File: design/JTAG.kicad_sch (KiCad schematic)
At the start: 46 parts

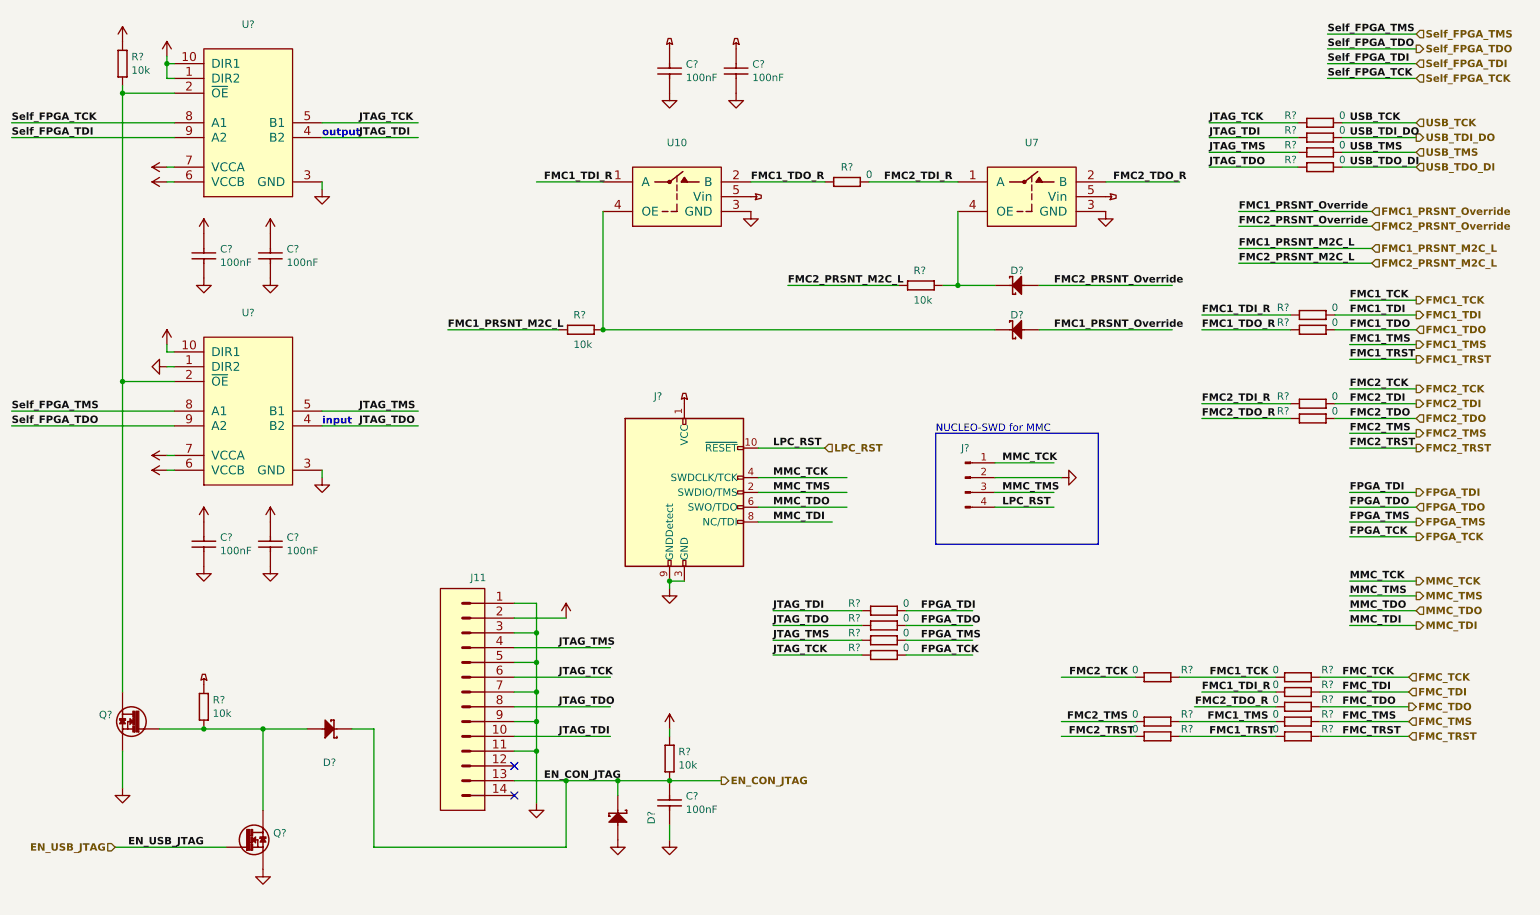
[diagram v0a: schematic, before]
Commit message: new power converter added
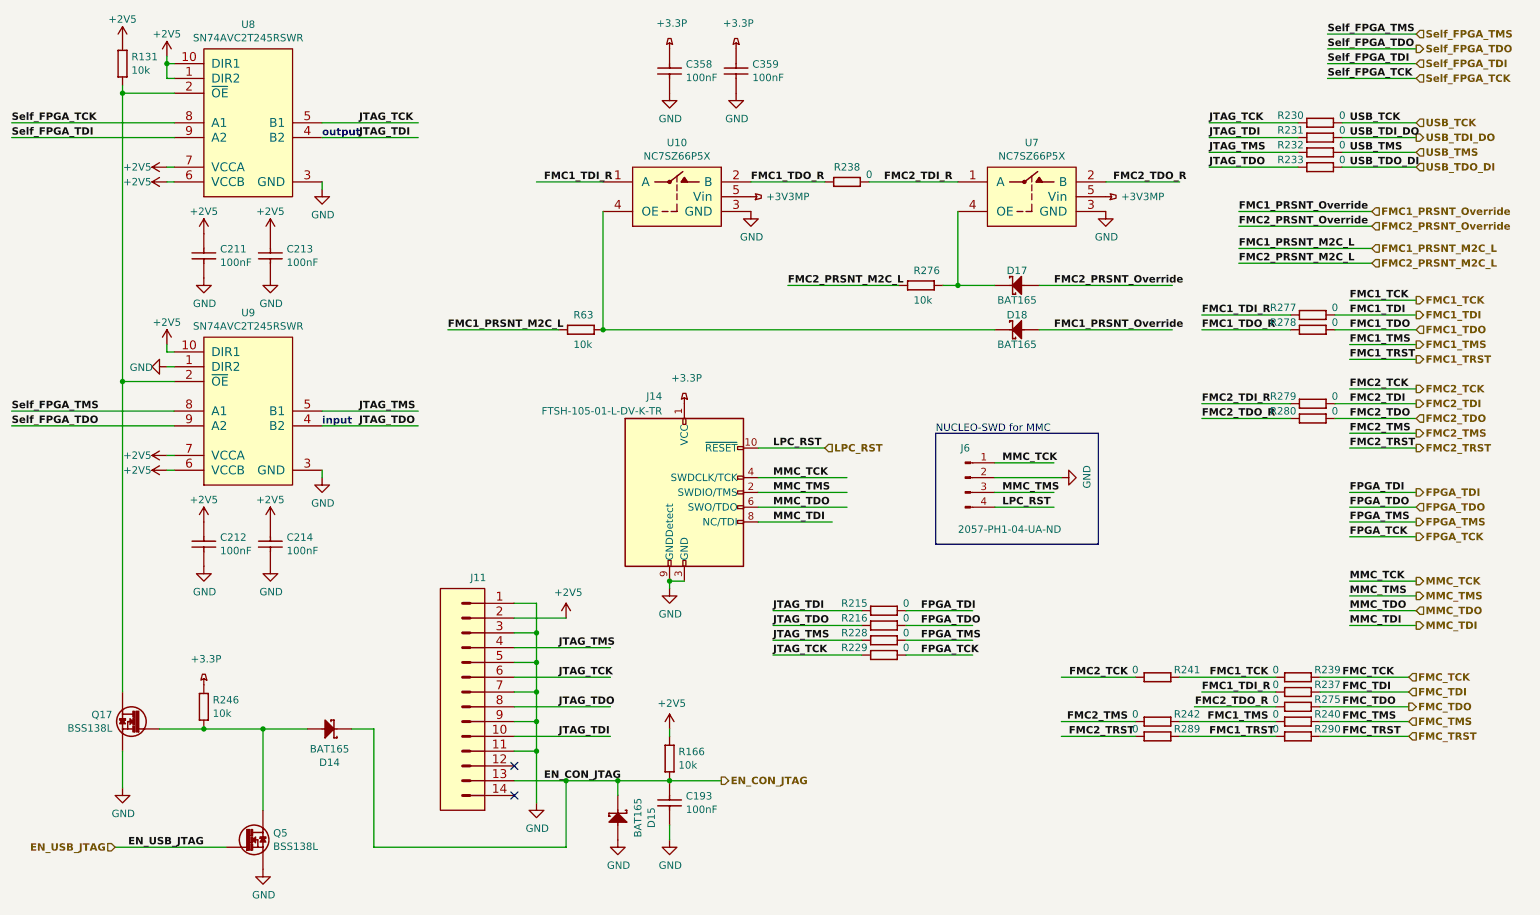
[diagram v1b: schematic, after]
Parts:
- C193, C211, C212, C213, C214, C358, C359: renamed from C?; value (none) -> CC0201_100NF_6.3V_10%_X5R; footprint (none) -> CAPC0603X33N
- D14, D15, D17, D18: renamed from D?; value (none) -> BAT165; footprint (none) -> ICs And Semiconductors SMD:SOD2512X110N
- J11: value (none) -> MOLEX_87831-1420; footprint (none) -> MOLEX THD:MOLEX_87831-1420
- J14: renamed from J?; value (none) -> FTSH-105-01-L-DV-K-TR; footprint (none) -> SAMTEC SMD:SAMTEC_FTSH-105-01-L-DV-K
- J6: renamed from J?; value (none) -> 2057-PH1-04-UA-ND; footprint (none) -> Connectors THD:SAMTEC_MTLW-104-07-L-S-250
- Q17, Q5: renamed from Q?; value (none) -> BSS138L; footprint (none) -> ICs And Semiconductors SMD:SOT95P240X110-3N
- R131, R166, R246, R276, R63: renamed from R?; value (none) -> R0402_10K_1%_0.0625W_100PPM; footprint (none) -> RESC1005X40N
- R215, R216, R228, R229, R230, R231, R232, R233, R237, R238, R239, R240, R241, R242, R275, R277, R278, R279, R280, R289, R290: renamed from R?; value (none) -> R0402_0R_JUMPER; footprint (none) -> RESC1005X40N
- U10, U7: value (none) -> NC7SZ66P5X; footprint (none) -> SOT65P210X110-5N
- U8, U9: renamed from U?; value (none) -> SN74AVC2T245RSWR; footprint (none) -> ICs And Semiconductors SMD:QFN40P140X180X55-10N

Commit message: connected signals to the J9 connector
connected signals to the J9 connector
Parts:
- C193, C211, C212, C213, C214, C358, C359, J11, R131, R166, R215, R216, R228, R229, R230, R231, R232, R233, R237, R238, R239, R240, R241, R242, R246, R275, R276, R277, R278, R279, R280, R289, R290, R63: Author CERN DEM JLC -> (none)
- D14, D15, D17, D18, Q17, Q5, U10, U7, U8, U9: Author CERN DEM JLC -> (none); Bonding No -> (none)

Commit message: Attempt to add and improve BOM. Added new part numbers for some of the passives
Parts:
- R215, R216, R228, R229, R230, R231, R232, R233, R237, R238, R239, R240, R241, R242, R275, R277, R278, R279, R280, R289, R290: MANUFACTURER (none) -> GENERIC
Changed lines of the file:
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@@
       (effects (font (size 1.524 1.524)) (justify left) hide)
     )
+    (property "MANUFACTURER" "GENERIC" (id 41) (at 179.07 123.19 0)
+      (effects (font (size 1.27 1.27)) hide)
+    )
     (pin "1")
     (pin "2")
@@
       (effects (font (size 1.524 1.524)) (justify left) hide)
     )
+    (property "MANUFACTURER" "GENERIC" (id 41) (at 179.07 125.73 0)
+      (effects (font (size 1.27 1.27)) hide)
+    )
     (pin "1")
     (pin "2")
@@
       (effects (font (size 1.524 1.524)) (justify left) hide)
     )
+    (property "MANUFACTURER" "GENERIC" (id 41) (at 179.07 128.27 0)
+      (effects (font (size 1.27 1.27)) hide)
+    )
     (pin "1")
     (pin "2")
@@
       (effects (font (size 1.524 1.524)) (justify left) hide)
     )
+    (property "MANUFACTURER" "GENERIC" (id 41) (at 179.07 130.81 0)
+      (effects (font (size 1.27 1.27)) hide)
+    )
     (pin "1")
     (pin "2")
@@
       (effects (font (size 1.524 1.524)) (justify left) hide)
     )
+    (property "MANUFACTURER" "GENERIC" (id 41) (at 254 41.91 0)
+      (effects (font (size 1.27 1.27)) hide)
+    )
     (pin "1")
     (pin "2")
@@
       (effects (font (size 1.524 1.524)) (justify left) hide)
     )
+    (property "MANUFACTURER" "GENERIC" (id 41) (at 254 46.99 0)
+      (effects (font (size 1.27 1.27)) hide)
+    )
     (pin "1")
     (pin "2")
@@
       (effects (font (size 1.524 1.524)) (justify left) hide)
     )
+    (property "MANUFACTURER" "GENERIC" (id 41) (at 254 44.45 0)
+      (effects (font (size 1.27 1.27)) hide)
+    )
     (pin "1")
     (pin "2")
@@
       (effects (font (size 1.524 1.524)) (justify left) hide)
     )
+    (property "MANUFACTURER" "GENERIC" (id 41) (at 254 39.37 0)
+      (effects (font (size 1.27 1.27)) hide)
+    )
     (pin "1")
     (pin "2")
@@
       (effects (font (size 1.524 1.524)) (justify left) hide)
     )
+    (property "MANUFACTURER" "GENERIC" (id 41) (at 172.72 49.53 0)
+      (effects (font (size 1.27 1.27)) hide)
+    )
     (pin "1")
     (pin "2")
@@
       (effects (font (size 1.524 1.524)) (justify left) hide)
     )
+    (property "MANUFACTURER" "GENERIC" (id 41) (at 250.19 137.16 0)
+      (effects (font (size 1.27 1.27)) hide)
+    )
     (pin "1")
     (pin "2")
@@
       (effects (font (size 1.524 1.524)) (justify left) hide)
     )
+    (property "MANUFACTURER" "GENERIC" (id 41) (at 242.57 134.62 0)
+      (effects (font (size 1.27 1.27)) hide)
+    )
     (pin "1")
     (pin "2")
@@
       (effects (font (size 1.524 1.524)) (justify left) hide)
     )
+    (property "MANUFACTURER" "GENERIC" (id 41) (at 218.44 134.62 0)
+      (effects (font (size 1.27 1.27)) hide)
+    )
     (pin "1")
     (pin "2")
@@
       (effects (font (size 1.524 1.524)) (justify left) hide)
     )
+    (property "MANUFACTURER" "GENERIC" (id 41) (at 242.57 142.24 0)
+      (effects (font (size 1.27 1.27)) hide)
+    )
     (pin "1")
     (pin "2")
@@
       (effects (font (size 1.524 1.524)) (justify left) hide)
     )
+    (property "MANUFACTURER" "GENERIC" (id 41) (at 218.44 142.24 0)
+      (effects (font (size 1.27 1.27)) hide)
+    )
     (pin "1")
     (pin "2")
@@
       (effects (font (size 1.524 1.524)) (justify left) hide)
     )
+    (property "MANUFACTURER" "GENERIC" (id 41) (at 242.57 144.78 0)
+      (effects (font (size 1.27 1.27)) hide)
+    )
     (pin "1")
     (pin "2")
@@
       (effects (font (size 1.524 1.524)) (justify left) hide)
     )
+    (property "MANUFACTURER" "GENERIC" (id 41) (at 218.44 144.78 0)
+      (effects (font (size 1.27 1.27)) hide)
+    )
     (pin "1")
     (pin "2")
@@
       (effects (font (size 1.524 1.524)) (justify left) hide)
     )
+    (property "MANUFACTURER" "GENERIC" (id 41) (at 242.57 139.7 0)
+      (effects (font (size 1.27 1.27)) hide)
+    )
     (pin "1")
     (pin "2")
@@
       (effects (font (size 1.524 1.524)) (justify left) hide)
     )
+    (property "MANUFACTURER" "GENERIC" (id 41) (at 252.73 72.39 0)
+      (effects (font (size 1.27 1.27)) hide)
+    )
     (pin "1")
     (pin "2")
@@
       (effects (font (size 1.524 1.524)) (justify left) hide)
     )
+    (property "MANUFACTURER" "GENERIC" (id 41) (at 252.73 74.93 0)
+      (effects (font (size 1.27 1.27)) hide)
+    )
     (pin "1")
     (pin "2")
@@
       (effects (font (size 1.524 1.524)) (justify left) hide)
     )
+    (property "MANUFACTURER" "GENERIC" (id 41) (at 252.73 87.63 0)
+      (effects (font (size 1.27 1.27)) hide)
+    )
     (pin "1")
     (pin "2")
@@
       (effects (font (size 1.524 1.524)) (justify left) hide)
     )
+    (property "MANUFACTURER" "GENERIC" (id 41) (at 252.73 90.17 0)
+      (effects (font (size 1.27 1.27)) hide)
+    )
     (pin "1")

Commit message: Restore some consistency in schematic metadata
Still 13 problematic footprint names in LTM4673.kicad_sch:

BAD Dup: "Footprint" "CAPC1608X87N" "Capacitors SMD:CAPC1005X55N" in LTM4673-altium-import:0_Capacitor - non polarized
BAD Dup: "Footprint" "CAPC2012X135N" "CAPC1608X87N" in LTM4673-altium-import:1_Capacitor - non polarized
BAD Dup: "Footprint" "CAPC1608X87N" "Capacitors SMD:CAPC1005X55N" in LTM4673-altium-import:1_Capacitor - non polarized
BAD Dup: "Footprint" "CAPC3216X180N" "CAPC3225X270N" in LTM4673-altium-import:1_Capacitor - non polarized
BAD Dup: "Footprint" "CAPC1608X87N" "Capacitors SMD:CAPC1005X55N" in LTM4673-altium-import:0_Capacitor - non polarized
BAD Dup: "Footprint" "CAPC1608X87N" "Capacitors SMD:CAPC1005X55N" in LTM4673-altium-import:0_Capacitor - non polarized
BAD Dup: "Footprint" "CAPC3216X180N" "CAPC3225X270N" in LTM4673-altium-import:1_Capacitor - non polarized
BAD Dup: "Footprint" "CAPC2012X135N" "CAPC1608X87N" in LTM4673-altium-import:1_Capacitor - non polarized
BAD Dup: "Footprint" "CAPC3216X180N" "CAPC3225X270N" in LTM4673-altium-import:1_Capacitor - non polarized
BAD Dup: "Footprint" "CAPC1608X87N" "Capacitors SMD:CAPC1005X55N" in LTM4673-altium-import:0_Capacitor - non polarized
BAD Dup: "Footprint" "CAPC1608X87N" "Capacitors SMD:CAPC1005X55N" in LTM4673-altium-import:1_Capacitor - non polarized
BAD Dup: "Footprint" "CAPC3216X180N" "CAPC3225X270N" in LTM4673-altium-import:1_Capacitor - non polarized
BAD Dup: "Footprint" "CAPMP7343X310N" "Capacitor_Tantalum_SMD:CP_EIA-7343-30_AVX-N" in LTM4673-altium-import:3_Capacitor - polarized

But the Symbol Field editor in eeschema should be more useful now.
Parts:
- R215, R216, R228, R229, R230, R231, R232, R233, R237, R238, R239, R240, R241, R242, R275, R277, R278, R279, R280, R289, R290: MANUFACTURER GENERIC -> (none)
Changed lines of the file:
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@@
       (effects (font (size 1.524 1.524)) (justify left) hide)
     )
-    (property "MANUFACTURER" "GENERIC" (id 41) (at 179.07 123.19 0)
-      (effects (font (size 1.27 1.27)) hide)
-    )
     (pin "1")
     (pin "2")
@@
       (effects (font (size 1.524 1.524)) (justify left) hide)
     )
-    (property "MANUFACTURER" "GENERIC" (id 41) (at 179.07 125.73 0)
-      (effects (font (size 1.27 1.27)) hide)
-    )
     (pin "1")
     (pin "2")
@@
       (effects (font (size 1.524 1.524)) (justify left) hide)
     )
-    (property "MANUFACTURER" "GENERIC" (id 41) (at 179.07 128.27 0)
-      (effects (font (size 1.27 1.27)) hide)
-    )
     (pin "1")
     (pin "2")
@@
       (effects (font (size 1.524 1.524)) (justify left) hide)
     )
-    (property "MANUFACTURER" "GENERIC" (id 41) (at 179.07 130.81 0)
-      (effects (font (size 1.27 1.27)) hide)
-    )
     (pin "1")
     (pin "2")
@@
       (effects (font (size 1.524 1.524)) (justify left) hide)
     )
-    (property "MANUFACTURER" "GENERIC" (id 41) (at 254 41.91 0)
-      (effects (font (size 1.27 1.27)) hide)
-    )
     (pin "1")
     (pin "2")
@@
       (effects (font (size 1.524 1.524)) (justify left) hide)
     )
-    (property "MANUFACTURER" "GENERIC" (id 41) (at 254 46.99 0)
-      (effects (font (size 1.27 1.27)) hide)
-    )
     (pin "1")
     (pin "2")
@@
       (effects (font (size 1.524 1.524)) (justify left) hide)
     )
-    (property "MANUFACTURER" "GENERIC" (id 41) (at 254 44.45 0)
-      (effects (font (size 1.27 1.27)) hide)
-    )
     (pin "1")
     (pin "2")
@@
       (effects (font (size 1.524 1.524)) (justify left) hide)
     )
-    (property "MANUFACTURER" "GENERIC" (id 41) (at 254 39.37 0)
-      (effects (font (size 1.27 1.27)) hide)
-    )
     (pin "1")
     (pin "2")
@@
       (effects (font (size 1.524 1.524)) (justify left) hide)
     )
-    (property "MANUFACTURER" "GENERIC" (id 41) (at 172.72 49.53 0)
-      (effects (font (size 1.27 1.27)) hide)
-    )
     (pin "1")
     (pin "2")
@@
       (effects (font (size 1.524 1.524)) (justify left) hide)
     )
-    (property "MANUFACTURER" "GENERIC" (id 41) (at 250.19 137.16 0)
-      (effects (font (size 1.27 1.27)) hide)
-    )
     (pin "1")
     (pin "2")
@@
       (effects (font (size 1.524 1.524)) (justify left) hide)
     )
-    (property "MANUFACTURER" "GENERIC" (id 41) (at 242.57 134.62 0)
-      (effects (font (size 1.27 1.27)) hide)
-    )
     (pin "1")
     (pin "2")
@@
       (effects (font (size 1.524 1.524)) (justify left) hide)
     )
-    (property "MANUFACTURER" "GENERIC" (id 41) (at 218.44 134.62 0)
-      (effects (font (size 1.27 1.27)) hide)
-    )
     (pin "1")
     (pin "2")
@@
       (effects (font (size 1.524 1.524)) (justify left) hide)
     )
-    (property "MANUFACTURER" "GENERIC" (id 41) (at 242.57 142.24 0)
-      (effects (font (size 1.27 1.27)) hide)
-    )
     (pin "1")
     (pin "2")
@@
       (effects (font (size 1.524 1.524)) (justify left) hide)
     )
-    (property "MANUFACTURER" "GENERIC" (id 41) (at 218.44 142.24 0)
-      (effects (font (size 1.27 1.27)) hide)
-    )
     (pin "1")
     (pin "2")
@@
       (effects (font (size 1.524 1.524)) (justify left) hide)
     )
-    (property "MANUFACTURER" "GENERIC" (id 41) (at 242.57 144.78 0)
-      (effects (font (size 1.27 1.27)) hide)
-    )
     (pin "1")
     (pin "2")
@@
       (effects (font (size 1.524 1.524)) (justify left) hide)
     )
-    (property "MANUFACTURER" "GENERIC" (id 41) (at 218.44 144.78 0)
-      (effects (font (size 1.27 1.27)) hide)
-    )
     (pin "1")
     (pin "2")
@@
       (effects (font (size 1.524 1.524)) (justify left) hide)
     )
-    (property "MANUFACTURER" "GENERIC" (id 41) (at 242.57 139.7 0)
-      (effects (font (size 1.27 1.27)) hide)
-    )
     (pin "1")
     (pin "2")
@@
       (effects (font (size 1.524 1.524)) (justify left) hide)
     )
-    (property "MANUFACTURER" "GENERIC" (id 41) (at 252.73 72.39 0)
-      (effects (font (size 1.27 1.27)) hide)
-    )
     (pin "1")
     (pin "2")
@@
       (effects (font (size 1.524 1.524)) (justify left) hide)
     )
-    (property "MANUFACTURER" "GENERIC" (id 41) (at 252.73 74.93 0)
-      (effects (font (size 1.27 1.27)) hide)
-    )
     (pin "1")
     (pin "2")
@@
       (effects (font (size 1.524 1.524)) (justify left) hide)
     )
-    (property "MANUFACTURER" "GENERIC" (id 41) (at 252.73 87.63 0)
-      (effects (font (size 1.27 1.27)) hide)
-    )
     (pin "1")
     (pin "2")
@@
       (effects (font (size 1.524 1.524)) (justify left) hide)
     )
-    (property "MANUFACTURER" "GENERIC" (id 41) (at 252.73 90.17 0)
-      (effects (font (size 1.27 1.27)) hide)
-    )
     (pin "1")

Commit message: Parts substitutions and a reproducibility tweak
INFINEON BAT165E6327HTSA1 becomes NEXPERIA BAT165AX (it was actually like this before)
Murata GRM155R61A225ME95D becomes Taiyo Yuden JMK105BJ225KV-F
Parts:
- D14, D15, D17, D18: Manufacturer INFINEON -> NEXPERIA; Manufacturer Part Number BAT165E6327HTSA1 -> BAT165AX
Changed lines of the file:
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@@
       (effects (font (size 1.524 1.524)) (justify left) hide)
     )
-    (property "Manufacturer" "INFINEON" (id 16) (at 172.212 162.56 0)
-      (effects (font (size 1.524 1.524)) (justify left) hide)
-    )
-    (property "Manufacturer Part Number" "BAT165E6327HTSA1" (id 17) (at 174.498 162.56 0)
+    (property "Manufacturer" "NEXPERIA" (id 16) (at 172.212 162.56 0)
+      (effects (font (size 1.524 1.524)) (justify left) hide)
+    )
+    (property "Manufacturer Part Number" "BAT165AX" (id 17) (at 174.498 162.56 0)
       (effects (font (size 1.524 1.524)) (justify left) hide)
     )
@@
       (effects (font (size 1.524 1.524)) (justify left) hide)
     )
-    (property "Manufacturer" "INFINEON" (id 16) (at 76.2 186.182 0)
-      (effects (font (size 1.524 1.524)) (justify left) hide)
-    )
-    (property "Manufacturer Part Number" "BAT165E6327HTSA1" (id 17) (at 76.2 188.468 0)
+    (property "Manufacturer" "NEXPERIA" (id 16) (at 76.2 186.182 0)
+      (effects (font (size 1.524 1.524)) (justify left) hide)
+    )
+    (property "Manufacturer Part Number" "BAT165AX" (id 17) (at 76.2 188.468 0)
       (effects (font (size 1.524 1.524)) (justify left) hide)
     )
@@
       (effects (font (size 1.524 1.524)) (justify left) hide)
     )
-    (property "Manufacturer" "INFINEON" (id 16) (at 201.93 24.638 0)
-      (effects (font (size 1.524 1.524)) (justify left) hide)
-    )
-    (property "Manufacturer Part Number" "BAT165E6327HTSA1" (id 17) (at 201.93 22.352 0)
+    (property "Manufacturer" "NEXPERIA" (id 16) (at 201.93 24.638 0)
+      (effects (font (size 1.524 1.524)) (justify left) hide)
+    )
+    (property "Manufacturer Part Number" "BAT165AX" (id 17) (at 201.93 22.352 0)
       (effects (font (size 1.524 1.524)) (justify left) hide)
     )
@@
       (effects (font (size 1.524 1.524)) (justify left) hide)
     )
-    (property "Manufacturer" "INFINEON" (id 16) (at 201.93 32.258 0)
-      (effects (font (size 1.524 1.524)) (justify left) hide)
-    )
-    (property "Manufacturer Part Number" "BAT165E6327HTSA1" (id 17) (at 201.93 29.972 0)
-      (effects (font (size 1.524 1.524)) (justify left) hide)
-    )
+    (property "Manufacturer" "NEXPERIA" (id 16) (at 201.93 32.258 0)
+      (effects (font (size 1.524 1.524)) (justify left) hide)
+    )
+    (property "Manufacturer Part Number" "BAT165AX" (id 17) (at 201.93 29.972 0)
+      (effects (font (size 1.524 1.524)) (justify left) hide)
+    )
